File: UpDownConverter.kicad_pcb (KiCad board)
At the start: 2 copper layers, 12 parts, among them IC1 ADE-2ASK+, J1 PCB.SMAFRA.HT, J2 PCB.SMAFRA.HT, J3 PCB.SMAFRA.HT

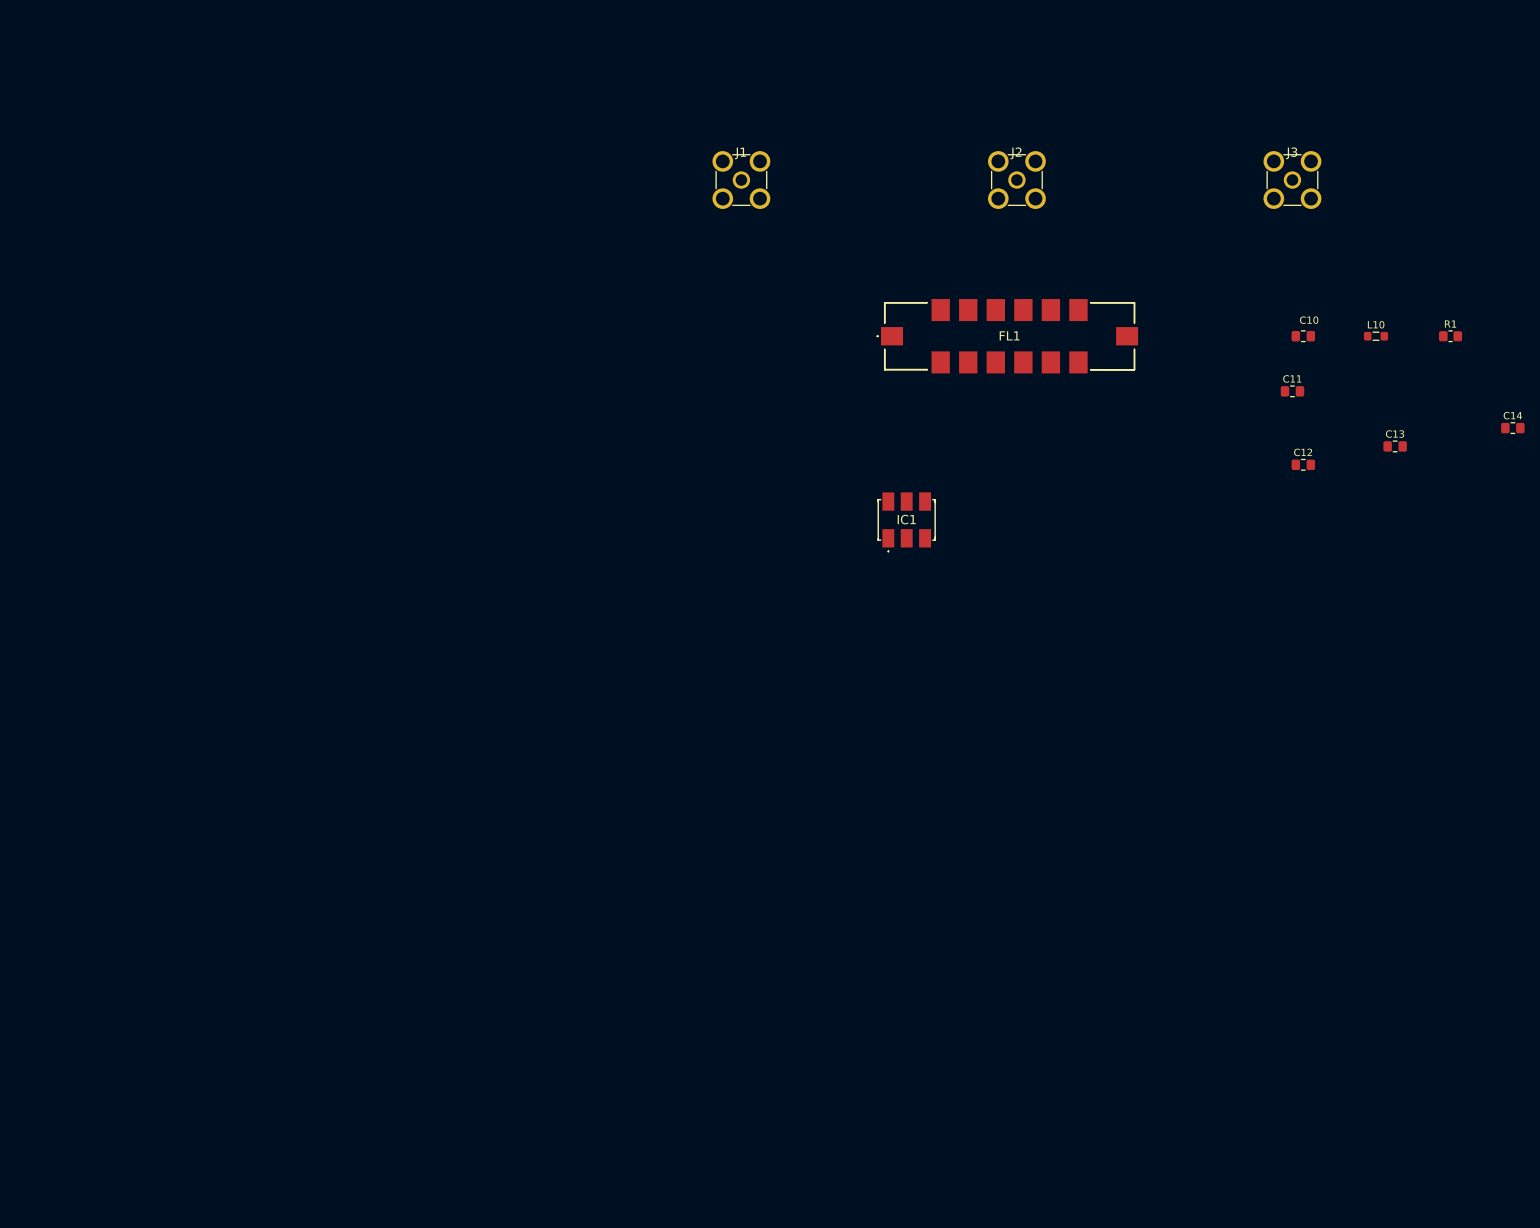
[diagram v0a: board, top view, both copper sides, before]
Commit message: Major restructure. Add power/control busses.
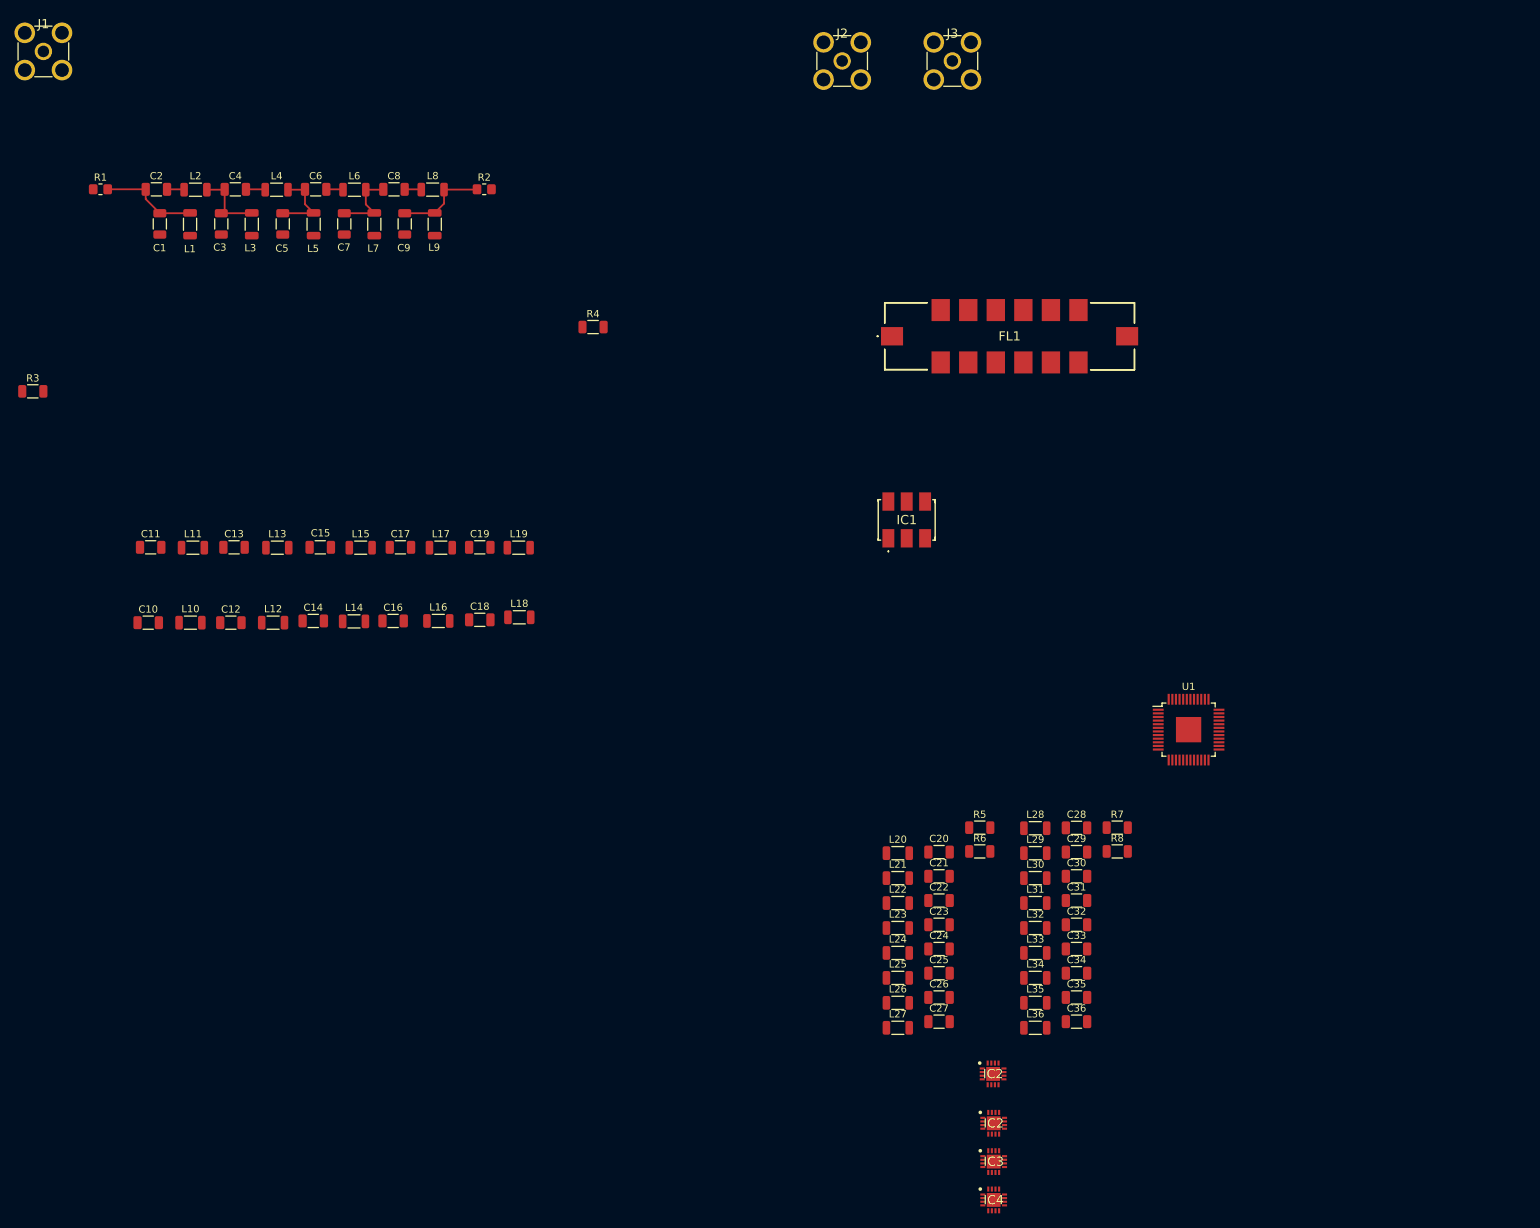
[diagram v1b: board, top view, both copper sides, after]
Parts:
- added C10: 18pF, Capacitor_SMD:C_1206_3216Metric, F.Cu at (37.4, 108.2)
- added C11: 68pf, Capacitor_SMD:C_1206_3216Metric, F.Cu at (37.7, 97.8)
- added C12: 33pF, Capacitor_SMD:C_1206_3216Metric, F.Cu at (48.8, 108.2)
- added C13: 56pF, Capacitor_SMD:C_1206_3216Metric, F.Cu at (49.2, 97.8)
- added C14: 33pF, Capacitor_SMD:C_1206_3216Metric, F.Cu at (60.2, 108.0)
- added C15: 56pF, Capacitor_SMD:C_1206_3216Metric, F.Cu at (61.1, 97.8)
- added C16: 33pF, Capacitor_SMD:C_1206_3216Metric, F.Cu at (71.2, 108.0)
- added C17: 68pF, Capacitor_SMD:C_1206_3216Metric, F.Cu at (72.2, 97.8)
- added C18: 18pF, Capacitor_SMD:C_1206_3216Metric, F.Cu at (83.2, 107.8)
- added C19: 4.7 pF, Capacitor_SMD:C_1206_3216Metric, F.Cu at (83.2, 97.8)
- added C20: 6.8 pf, Capacitor_SMD:C_1206_3216Metric, F.Cu at (146.7, 139.9)
- added C21: 8.2 pF, Capacitor_SMD:C_1206_3216Metric, F.Cu at (146.7, 143.3)
- added C22: 5.6 pF, Capacitor_SMD:C_1206_3216Metric, F.Cu at (146.7, 146.6)
- added C23: 8.2 pF, Capacitor_SMD:C_1206_3216Metric, F.Cu at (146.7, 150.0)
- added C24: 5.6 pF, Capacitor_SMD:C_1206_3216Metric, F.Cu at (146.7, 153.3)
- added C25: 8.2 pF, Capacitor_SMD:C_1206_3216Metric, F.Cu at (146.7, 156.7)
- added C26: 6.8 pF, Capacitor_SMD:C_1206_3216Metric, F.Cu at (146.7, 160.0)
- added C27: 4.7 pF, Capacitor_SMD:C_1206_3216Metric, F.Cu at (146.7, 163.4)
- added C28: 4.7 pF, Capacitor_SMD:C_1206_3216Metric, F.Cu at (165.7, 136.6)
- added C29: 6.8 pf, Capacitor_SMD:C_1206_3216Metric, F.Cu at (165.7, 139.9)
- added C30: 8.2 pF, Capacitor_SMD:C_1206_3216Metric, F.Cu at (165.7, 143.3)
- added C31: 5.6 pF, Capacitor_SMD:C_1206_3216Metric, F.Cu at (165.7, 146.6)
- added C32: 8.2 pF, Capacitor_SMD:C_1206_3216Metric, F.Cu at (165.7, 150.0)
- added C33: 5.6 pF, Capacitor_SMD:C_1206_3216Metric, F.Cu at (165.7, 153.3)
- added C34: 8.2 pF, Capacitor_SMD:C_1206_3216Metric, F.Cu at (165.7, 156.7)
- added C35: 6.8 pF, Capacitor_SMD:C_1206_3216Metric, F.Cu at (165.7, 160.0)
- added C36: 4.7 pF, Capacitor_SMD:C_1206_3216Metric, F.Cu at (165.7, 163.4)
- added C6: 680pF, Capacitor_SMD:C_1206_3216Metric, F.Cu at (60.5, 48.3)
- added C7: 180 pF, Capacitor_SMD:C_1206_3216Metric, F.Cu at (64.5, 53.0)
- added C8: 820pF, Capacitor_SMD:C_1206_3216Metric, F.Cu at (71.3, 48.3)
- added C9: 100 pF, Capacitor_SMD:C_1206_3216Metric, F.Cu at (72.8, 53.0)
- added IC2: HMC1118LP3DE, Mouser:QFN50P300X300X95-17N-D, F.Cu at (154.3, 177.4)
- added IC2: HMC1118LP3DE, Mouser:QFN50P300X300X95-17N-D, F.Cu at (154.2, 170.6)
- added IC3: HMC1118LP3DE, Mouser:QFN50P300X300X95-17N-D, F.Cu at (154.3, 182.7)
- added IC4: HMC1118LP3DE, Mouser:QFN50P300X300X95-17N-D, F.Cu at (154.3, 188.0)
- added L10: 180nH, Inductor_SMD:L_1206_3216Metric, F.Cu at (43.2, 108.2)
- added L11: 56nH, Inductor_SMD:L_1206_3216Metric, F.Cu at (43.5, 97.8)
- added L12: 100nH, Inductor_SMD:L_1206_3216Metric, F.Cu at (54.6, 108.2)
- added L13: 56nH, Inductor_SMD:L_1206_3216Metric, F.Cu at (55.2, 97.8)
- added L14: 100nH, Inductor_SMD:L_1206_3216Metric, F.Cu at (65.8, 108.0)
- added L15: 56nH, Inductor_SMD:L_1206_3216Metric, F.Cu at (66.7, 97.8)
- added L16: 100nH, Inductor_SMD:L_1206_3216Metric, F.Cu at (77.5, 108.0)
- added L17: 56 nH, Inductor_SMD:L_1206_3216Metric, F.Cu at (77.8, 97.8)
- added L18: 180nH, Inductor_SMD:L_1206_3216Metric, F.Cu at (88.7, 107.4)
- added L19: 22 nH, Inductor_SMD:L_1206_3216Metric, F.Cu at (88.6, 97.8)
- added L2: 330nH, Inductor_SMD:L_1206_3216Metric, F.Cu at (43.9, 48.3)
- added L20: 15 nH, Inductor_SMD:L_1206_3216Metric, F.Cu at (141.0, 140.1)
- added L21: 12 nH, Inductor_SMD:L_1206_3216Metric, F.Cu at (141.0, 143.5)
- added L22: 15 nH, Inductor_SMD:L_1206_3216Metric, F.Cu at (141.0, 147.0)
- added L23: 12 nH, Inductor_SMD:L_1206_3216Metric, F.Cu at (141.0, 150.4)
- added L24: 15 nH, Inductor_SMD:L_1206_3216Metric, F.Cu at (141.0, 153.9)
- added L25: 12 nH, Inductor_SMD:L_1206_3216Metric, F.Cu at (141.0, 157.3)
- added L26: 15 nH, Inductor_SMD:L_1206_3216Metric, F.Cu at (141.0, 160.8)
- added L27: 22 nH, Inductor_SMD:L_1206_3216Metric, F.Cu at (141.0, 164.2)
- added L28: 22 nH, Inductor_SMD:L_1206_3216Metric, F.Cu at (160.0, 136.6)
- added L29: 15 nH, Inductor_SMD:L_1206_3216Metric, F.Cu at (160.0, 140.1)
- added L3: 1.5 uH, Inductor_SMD:L_1206_3216Metric, F.Cu at (51.7, 53.1)
- added L30: 12 nH, Inductor_SMD:L_1206_3216Metric, F.Cu at (160.0, 143.5)
- added L31: 15 nH, Inductor_SMD:L_1206_3216Metric, F.Cu at (160.0, 147.0)
- added L32: 12 nH, Inductor_SMD:L_1206_3216Metric, F.Cu at (160.0, 150.4)
- added L33: 15 nH, Inductor_SMD:L_1206_3216Metric, F.Cu at (160.0, 153.9)
- added L34: 12 nH, Inductor_SMD:L_1206_3216Metric, F.Cu at (160.0, 157.3)
- added L35: 15 nH, Inductor_SMD:L_1206_3216Metric, F.Cu at (160.0, 160.8)
- added L36: 22 nH, Inductor_SMD:L_1206_3216Metric, F.Cu at (160.0, 164.2)
- added L4: 330nH, Inductor_SMD:L_1206_3216Metric, F.Cu at (55.1, 48.3)
- added L5: 1.5 uH, Inductor_SMD:L_1206_3216Metric, F.Cu at (60.2, 53.1)
- added L6: 330nH, Inductor_SMD:L_1206_3216Metric, F.Cu at (65.9, 48.3)
- added L7: 1.5 uH, Inductor_SMD:L_1206_3216Metric, F.Cu at (68.6, 53.1)
- added L8: 330nH, Inductor_SMD:L_1206_3216Metric, F.Cu at (76.7, 48.3)
- added L9: 2.7 uH, Inductor_SMD:L_1206_3216Metric, F.Cu at (77.0, 53.1)
- added R2: 50 Ohms, Resistor_SMD:R_0805_2012Metric_Pad1.20x1.40mm_HandSolder, F.Cu at (83.8, 48.3)
- added R3: 50 Ohms, Resistor_SMD:R_1206_3216Metric, F.Cu at (21.4, 76.2)
- added R4: 50 Ohms, Resistor_SMD:R_1206_3216Metric, F.Cu at (98.9, 67.3)
- added R5: 50 Ohms, Resistor_SMD:R_1206_3216Metric, F.Cu at (152.3, 136.5)
- added R6: 50 Ohms, Resistor_SMD:R_1206_3216Metric, F.Cu at (152.3, 139.8)
- added R7: 50 Ohms, Resistor_SMD:R_1206_3216Metric, F.Cu at (171.3, 136.5)
- added R8: 50 Ohms, Resistor_SMD:R_1206_3216Metric, F.Cu at (171.3, 139.8)
- added U1: AD9951, Package_QFP:TQFP-48-1EP_7x7mm_P0.5mm_EP3.5x3.5mm, F.Cu at (181.2, 123.0)
- C1: renamed from C10; value 150 pF -> 100 pF; footprint Capacitor_SMD:C_0805_2012Metric_Pad1.18x1.45mm_HandSolder -> Capacitor_SMD:C_1206_3216Metric
- C2: renamed from C11; value 680 pF -> 820pf; footprint Capacitor_SMD:C_0805_2012Metric_Pad1.18x1.45mm_HandSolder -> Capacitor_SMD:C_1206_3216Metric
- C3: renamed from C12; value 270 pF -> 180 pF; footprint Capacitor_SMD:C_0805_2012Metric_Pad1.18x1.45mm_HandSolder -> Capacitor_SMD:C_1206_3216Metric
- C4: renamed from C13; value 560 pF -> 680pF; footprint Capacitor_SMD:C_0805_2012Metric_Pad1.18x1.45mm_HandSolder -> Capacitor_SMD:C_1206_3216Metric
- C5: renamed from C14; value 270 pF -> 180 pF; footprint Capacitor_SMD:C_0805_2012Metric_Pad1.18x1.45mm_HandSolder -> Capacitor_SMD:C_1206_3216Metric
- L1: renamed from L10; value 1.8 uH -> 2.7 uH; footprint Inductor_SMD:L_0805_2012Metric_Pad1.05x1.20mm_HandSolder -> Inductor_SMD:L_1206_3216Metric
- moved R1 187.8 mm to (30.8, 48.3)
- moved C5 172.4 mm to (56.0, 53.0), turned to -90 degrees
- moved L1 164.7 mm to (43.1, 53.1), turned to -90 degrees
- moved C4 164.3 mm to (49.4, 48.3)
- moved C2 159.6 mm to (38.5, 48.3)
- moved C1 158.9 mm to (39.0, 53.0), turned to -90 degrees
- moved C3 153.3 mm to (47.5, 53.0), turned to -90 degrees
- moved J1 98.1 mm to (22.9, 29.2)
- moved J3 49.8 mm to (148.6, 30.5)
- moved J2 29.2 mm to (133.3, 30.5)
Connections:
- C1 pad 1: /HF_Bandpass_Filter/HF_BP_In -> Net-(C1-Pad1)
- C2 pad 1: /HF_Bandpass_Filter/HF_BP_In -> Net-(C1-Pad1)
- L1 pad 1: /HF_Bandpass_Filter/HF_BP_In -> Net-(C1-Pad1)
- R1 pad 2: Earth -> Net-(C1-Pad1)
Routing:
- net Net-(C1-Pad1): track 0.00 -> 13.6 mm
- net Net-(C9-Pad1): track 0.00 -> 12.5 mm
- net Net-(C5-Pad1): track 0.00 -> 10.4 mm
- net Net-(C7-Pad1): track 0.00 -> 10.3 mm
- net Net-(C3-Pad1): track 0.00 -> 10.2 mm
- net Net-(C4-Pad2): track 0.00 -> 2.68 mm
- net Net-(C2-Pad2): track 0.00 -> 2.38 mm
- net Net-(C6-Pad2): track 0.00 -> 2.33 mm
- net Net-(C8-Pad2): track 0.00 -> 2.31 mm
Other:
- copper layers 2 -> 4

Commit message: Add some of the routing for the power signals.
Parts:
- removed J1: PCB.SMAFRA.HT, SamacSys_Parts:PCBSMAFRAHT
- added IC5: ADRF5040BCPZ-R7, Mouser:QFN50P400X400X90-25N-D, F.Cu at (261.6, 54.6)
- added IC6: HMC1118LP3DE, Mouser:QFN50P300X300X95-17N-D, F.Cu at (261.9, 65.5)
- added J5: PCB.SMAFRA.HT, Mouser:PCBSMAFRAHT, F.Cu at (230.5, 63.7)
- C10, C18: value 18pF -> 18 pF
- C11: value 68pf -> 68 pf
- C12, C14, C16: value 33pF -> 33 pF
- C13, C15: value 56pF -> 56 pF
- C17: value 68pF -> 68 pF
- C2: value 820pf -> 820 pf
- C4, C6: value 680pF -> 680 pF
- C8: value 820pF -> 820 pF
- FL1: footprint SamacSys_Parts:BPFA410 -> Mouser:BPFA410
- IC1: footprint SamacSys_Parts:ADE2ASK -> Mouser:ADE2ASK
- J2, J3: footprint SamacSys_Parts:PCBSMAFRAHT -> Mouser:PCBSMAFRAHT
- L10, L18: value 180nH -> 180 nH
- L11, L13, L15: value 56nH -> 56 nH
- L12, L14, L16: value 100nH -> 100 nH
- L2, L4, L6, L8: value 330nH -> 330 nH
- moved J3 100.6 mm to (243.6, 63.7)
- moved IC1 90.6 mm to (217.3, 43.2)
- moved J2 90.4 mm to (217.4, 63.7)
- moved FL1 83.6 mm to (231.2, 31.1)
- moved U1 66.8 mm to (248.0, 124.1)
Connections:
- net /LBAND_Bandpass_Filter/L_Band_BP_Out renamed /LBAND_Bandpass_Filter/LBand BPF Port 2
- FL1 pad 10: Earth -> GND
- FL1 pad 11: Earth -> GND
- FL1 pad 12: Earth -> GND
- FL1 pad 13: Earth -> GND
- FL1 pad 14: Earth -> GND
- FL1 pad 2: Earth -> GND
- FL1 pad 3: Earth -> GND
- FL1 pad 4: Earth -> GND
- FL1 pad 5: Earth -> GND
- FL1 pad 6: Earth -> GND
- FL1 pad 7: Earth -> GND
- FL1 pad 9: Earth -> GND
- IC1 pad 1: Earth -> GND
- IC1 pad 3: unconnected-(IC1-RF-Pad3) -> Net-(IC1-RF)
- IC1 pad 4: Earth -> GND
- IC1 pad 5: Earth -> GND
- IC1 pad 6: Net-(IC1-LO) -> unconnected-(IC1-LO-Pad6)
- IC2 pad 1: Earth -> GND
- IC2 pad 10: unconnected-(IC2-VCTRL-Pad10) -> /Band Select Logic/CTRL2
- IC2 pad 11: unconnected-(IC2-LS-Pad11) -> /Band Select Logic/CTRL2
- IC2 pad 12: unconnected-(IC2-VDD-Pad12) -> /Band Select Logic/POWER1
- IC2 pad 13: Earth -> GND
- IC2 pad 14: /HF_Bandpass_Filter/HF_BP_Out -> /HF_Bandpass_Filter/HF BPF Port 2
- IC2 pad 15: Earth -> GND
- IC2 pad 16: Earth -> GND
- IC2 pad 17: Earth -> GND
- IC2 pad 2: Earth -> GND
- IC2 pad 4: Earth -> GND
- IC2 pad 5: Earth -> GND
- IC2 pad 6: Earth -> GND
- IC2 pad 8: Earth -> GND
- IC2 pad 9: unconnected-(IC2-VSS-Pad9) -> /Band Select Logic/POWER3
- IC3 pad 1: Earth -> GND
- IC3 pad 10: unconnected-(IC3-VCTRL-Pad10) -> /Band Select Logic/CTRL4
- IC3 pad 11: unconnected-(IC3-LS-Pad11) -> /Band Select Logic/CTRL4
- IC3 pad 12: unconnected-(IC3-VDD-Pad12) -> /Band Select Logic/POWER1
- IC3 pad 13: Earth -> GND
- IC3 pad 15: Earth -> GND
- IC3 pad 16: Earth -> GND
- IC3 pad 17: Earth -> GND
- IC3 pad 2: Earth -> GND
- IC3 pad 3: /Mixer & Band Select/Mixer_Common -> /Baseband TR Switch/Common
- IC3 pad 4: Earth -> GND
- IC3 pad 5: Earth -> GND
- IC3 pad 6: Earth -> GND
- IC3 pad 8: Earth -> GND
- IC3 pad 9: unconnected-(IC3-VSS-Pad9) -> /Band Select Logic/POWER3
- IC4 pad 1: Earth -> GND
- IC4 pad 10: unconnected-(IC4-VCTRL-Pad10) -> /Band Select Logic/CTRL3
- IC4 pad 11: unconnected-(IC4-LS-Pad11) -> /Band Select Logic/CTRL3
- IC4 pad 12: unconnected-(IC4-VDD-Pad12) -> /Band Select Logic/POWER1
- IC4 pad 13: Earth -> GND
- IC4 pad 15: Earth -> GND
- IC4 pad 16: Earth -> GND
- IC4 pad 17: Earth -> GND
- IC4 pad 2: Earth -> GND
- IC4 pad 4: Earth -> GND
- IC4 pad 5: Earth -> GND
- IC4 pad 6: Earth -> GND
- IC4 pad 8: Earth -> GND
- IC4 pad 9: unconnected-(IC4-VSS-Pad9) -> /Band Select Logic/POWER3
- J2 pad 1: Net-(IC1-LO) -> /Baseband TR Switch/TX
- J2 pad 2: Earth -> GND
- J2 pad 3: Earth -> GND
- J2 pad 4: Earth -> GND
- J2 pad 5: Earth -> GND
- J3 pad 1: Net-(FL1-RF_OUT) -> /Antenna/Antenna
- J3 pad 2: Earth -> GND
- J3 pad 3: Earth -> GND
- J3 pad 4: Earth -> GND
- J3 pad 5: Earth -> GND
- R1 pad 1: /HF_Bandpass_Filter/HF_BP_In -> /Band Select Switch/HF_Band
- R2 pad 2: /HF_Bandpass_Filter/HF_BP_Out -> /HF_Bandpass_Filter/HF BPF Port 2
- R3 pad 1: /VHF_Bandpass_Filter/VHF_BP_In -> /Band Select Switch/VHF Band
- R5 pad 1: /UHF_Bandpass_Filter/UHF_BP_In -> /Band Select Switch/UHF Band
- R7 pad 1: /LBAND_Bandpass_Filter/L_Band_BP_In -> /Band Select Switch/L Band Port
- U1 pad 14: unconnected-(U1-AGND-Pad14) -> GND
- U1 pad 15: unconnected-(U1-AGND-Pad15) -> GND
- U1 pad 17: unconnected-(U1-AGND-Pad17) -> GND
- U1 pad 22: unconnected-(U1-AGND-Pad22) -> GND
- U1 pad 26: unconnected-(U1-AGND-Pad26) -> GND
- U1 pad 28: unconnected-(U1-AGND-Pad28) -> GND
- U1 pad 3: unconnected-(U1-DGND-Pad3) -> GNDD
- U1 pad 30: unconnected-(U1-AGND-Pad30) -> GND
- U1 pad 31: unconnected-(U1-AGND-Pad31) -> GND
- U1 pad 32: unconnected-(U1-AGND-Pad32) -> GND
- U1 pad 33: unconnected-(U1-DGND-Pad33) -> GNDD
- U1 pad 42: unconnected-(U1-DGND-Pad42) -> GNDD
- U1 pad 47: unconnected-(U1-DGND-Pad47) -> GNDD
- U1 pad 48: unconnected-(U1-DGND-Pad48) -> GNDD
- U1 pad 5: unconnected-(U1-AGND-Pad5) -> GND
- U1 pad 7: unconnected-(U1-AGND-Pad7) -> GND
